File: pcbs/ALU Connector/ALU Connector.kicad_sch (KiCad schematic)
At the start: 4 parts

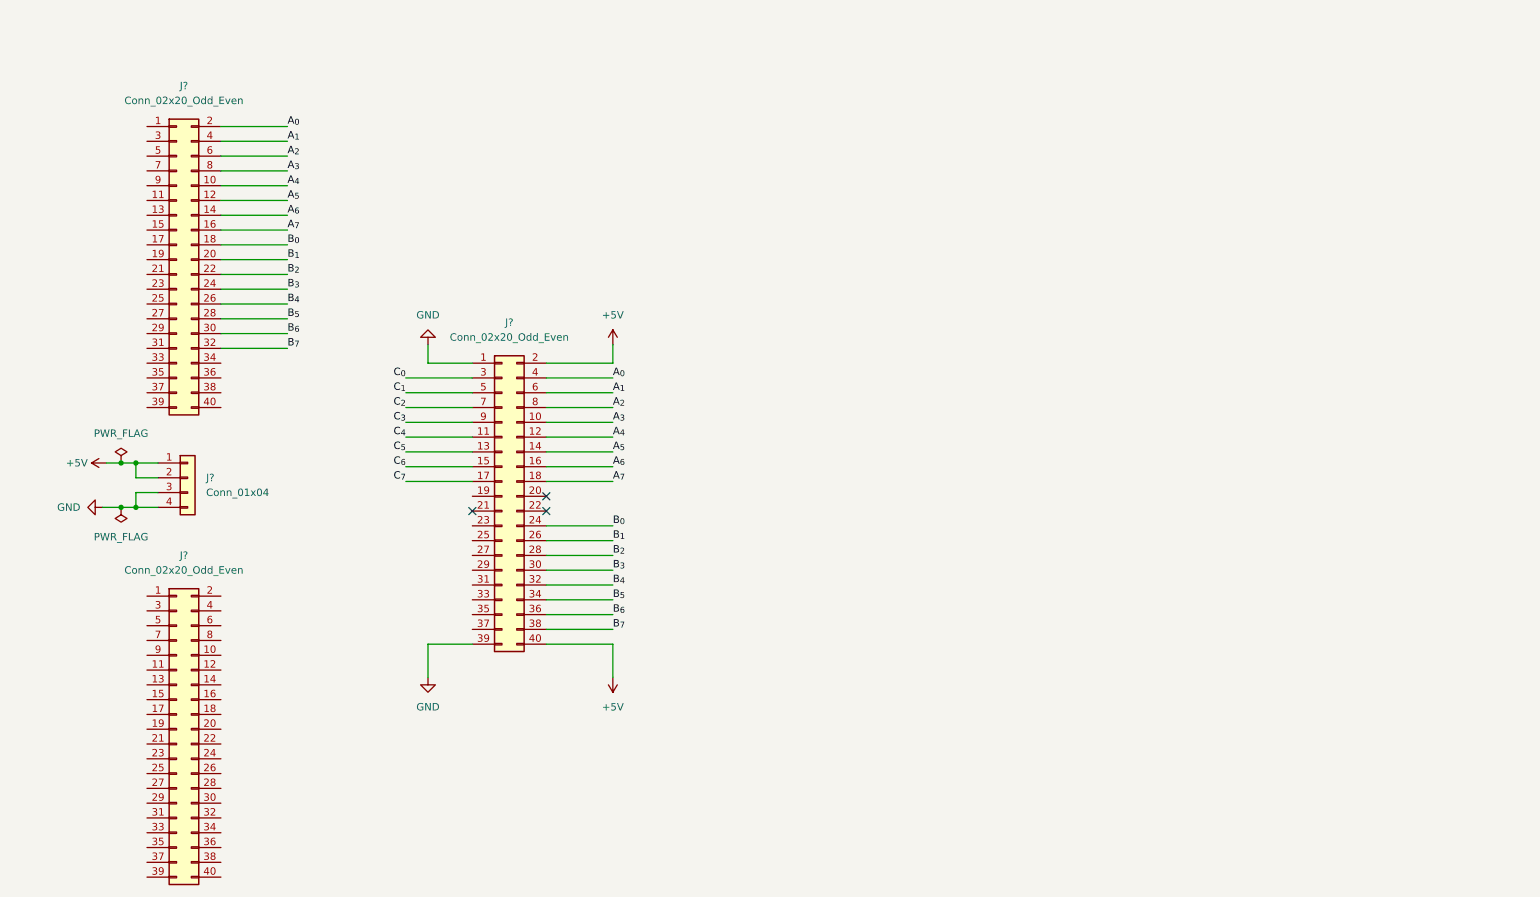
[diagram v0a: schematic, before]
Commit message: Some basic routing
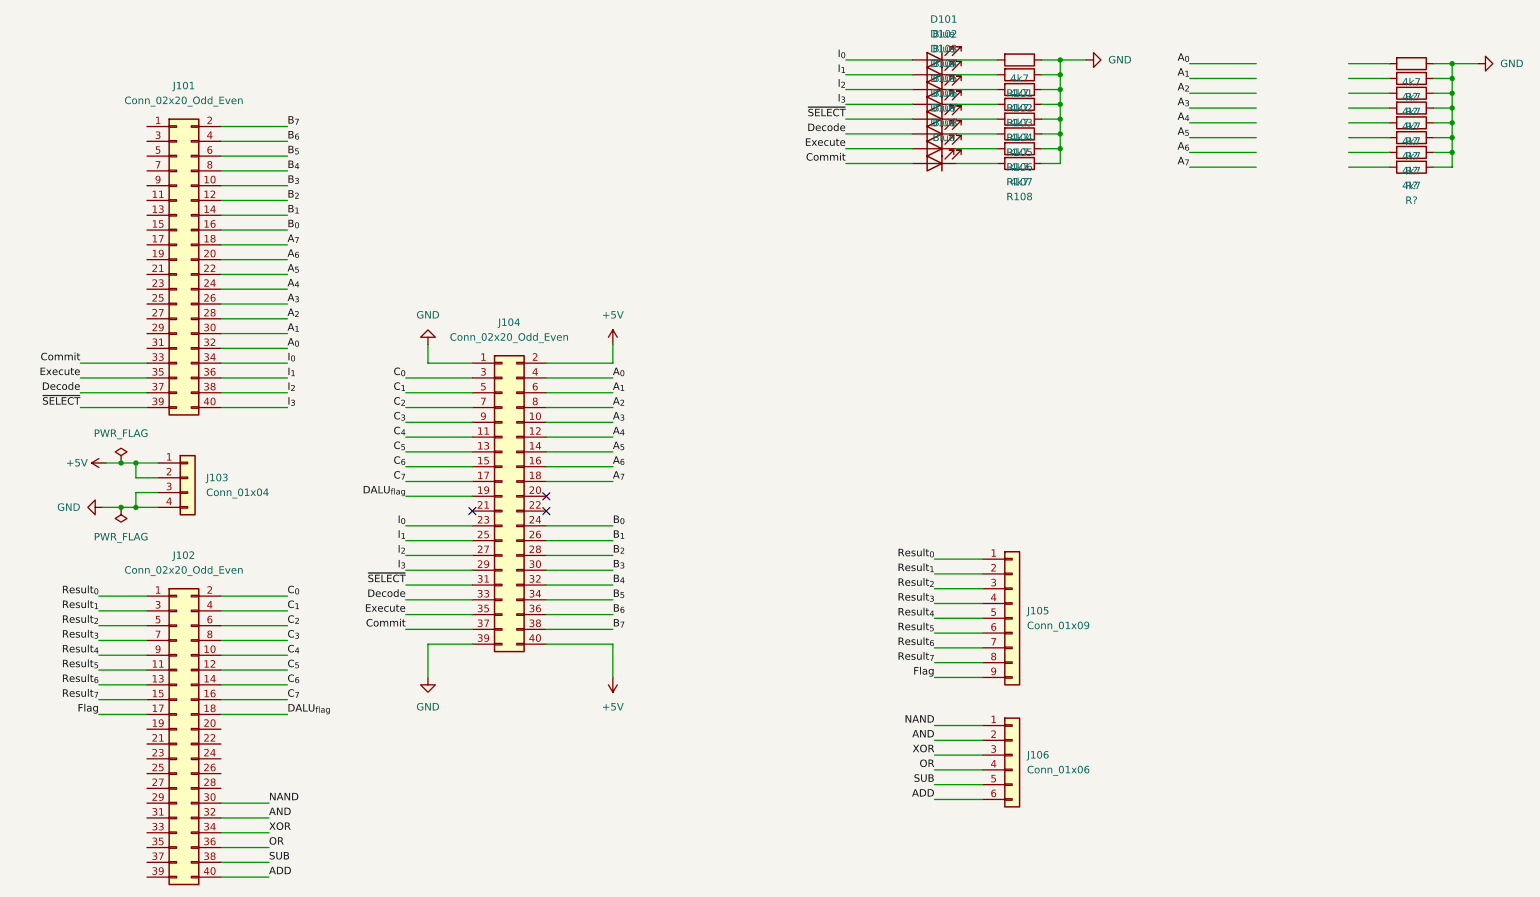
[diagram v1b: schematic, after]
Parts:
- added D101, D102, D103, D104, D105, D106, D107, D108: Blue, LED_SMD:LED_0603_1608Metric, symbol Device:LED
- added J105: Conn_01x09, Connector_PinHeader_2.54mm:PinHeader_1x09_P2.54mm_Vertical, symbol Connector_Generic:Conn_01x09
- added J106: Conn_01x06, Connector_PinHeader_2.54mm:PinHeader_1x06_P2.54mm_Vertical, symbol Connector_Generic:Conn_01x06
- added R101, R102, R103, R104, R105, R106, R107, R108, R? (x8): 4k7, Resistor_SMD:R_0603_1608Metric, symbol Device:R
- J101: renamed from J?; footprint (none) -> Connector_PinHeader_2.54mm:PinHeader_2x20_P2.54mm_Vertical
- J103: renamed from J?; footprint (none) -> Connector_PinHeader_2.54mm:PinHeader_1x04_P2.54mm_Vertical
- gave numbers to parts that had none: 2
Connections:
- net A_{0}: now also J101.32 (Pin_32); no longer J101.2 (Pin_2)
- net A_{1}: now also J101.30 (Pin_30); no longer J101.4 (Pin_4)
- net A_{2}: now also J101.28 (Pin_28); no longer J101.6 (Pin_6)
- net A_{3}: now also J101.26 (Pin_26); no longer J101.8 (Pin_8)
- net A_{4}: now also J101.24 (Pin_24); no longer J101.10 (Pin_10)
- net A_{5}: now also J101.22 (Pin_22); no longer J101.12 (Pin_12)
- net A_{6}: now also J101.20 (Pin_20); no longer J101.14 (Pin_14)
- net A_{7}: now also J101.18 (Pin_18); no longer J101.16 (Pin_16)
- net B_{0}: now also J101.16 (Pin_16); no longer J101.18 (Pin_18)
- net B_{1}: now also J101.14 (Pin_14); no longer J101.20 (Pin_20)
- net B_{2}: now also J101.12 (Pin_12); no longer J101.22 (Pin_22)
- net B_{3}: now also J101.10 (Pin_10); no longer J101.24 (Pin_24)
- net B_{4}: now also J101.8 (Pin_8); no longer J101.26 (Pin_26)
- net B_{5}: now also J101.6 (Pin_6); no longer J101.28 (Pin_28)
- net B_{6}: now also J101.4 (Pin_4); no longer J101.30 (Pin_30)
- net B_{7}: now also J101.2 (Pin_2); no longer J101.32 (Pin_32)
- net C_{0}: now also J102.2 (Pin_2)
- net C_{1}: now also J102.4 (Pin_4)
- net C_{2}: now also J102.6 (Pin_6)
- net C_{3}: now also J102.8 (Pin_8)
- net C_{4}: now also J102.10 (Pin_10)
- net C_{5}: now also J102.12 (Pin_12)
- net C_{6}: now also J102.14 (Pin_14)
- net C_{7}: now also J102.16 (Pin_16)
- net GND: now also R101.1, R102.1, R103.1, R104.1, R105.1, R106.1, R107.1, R108.1, R?.1, R?.1, R?.1, R?.1, R?.1, R?.1, R?.1, R?.1
- net Result_{0}: now reaches J102.1 (Pin_1)
- net Result_{0}: now also J105.1 (Pin_1)
- net Result_{5}: now reaches J102.11 (Pin_11)
- net Result_{5}: now also J105.6 (Pin_6)
- net Result_{6}: now reaches J102.13 (Pin_13)
- net Result_{6}: now also J105.7 (Pin_7)
- net Result_{7}: now reaches J102.15 (Pin_15)
- net Result_{7}: now also J105.8 (Pin_8)
- net Flag: now reaches J102.17 (Pin_17)
- net Flag: now also J105.9 (Pin_9)
- net DALU_{flag}: now reaches J102.18 (Pin_18)
- net DALU_{flag}: now also J104.19 (Pin_19)
- net Result_{1}: now reaches J102.3 (Pin_3)
- net Result_{1}: now also J105.2 (Pin_2)
- net NAND: now reaches J102.30 (Pin_30)
- net NAND: now also J106.1 (Pin_1)
- net AND: now reaches J102.32 (Pin_32)
- net AND: now also J106.2 (Pin_2)
- net XOR: now reaches J102.34 (Pin_34)
- net XOR: now also J106.3 (Pin_3)
- net OR: now reaches J102.36 (Pin_36)
- net OR: now also J106.4 (Pin_4)
- net SUB: now reaches J102.38 (Pin_38)
- net SUB: now also J106.5 (Pin_5)
- net ADD: now reaches J102.40 (Pin_40)
- net ADD: now also J106.6 (Pin_6)
- net Result_{2}: now reaches J102.5 (Pin_5)
- net Result_{2}: now also J105.3 (Pin_3)
- net Result_{3}: now reaches J102.7 (Pin_7)
- net Result_{3}: now also J105.4 (Pin_4)
- net Result_{4}: now reaches J102.9 (Pin_9)
- net Result_{4}: now also J105.5 (Pin_5)
- net I_{0}: now reaches J104.23 (Pin_23)
- net I_{0}: now also J101.34 (Pin_34), D101.2 (A)
- net I_{1}: now reaches J104.25 (Pin_25)
- net I_{1}: now also J101.36 (Pin_36), D102.2 (A)
- net I_{2}: now reaches J104.27 (Pin_27)
- net I_{2}: now also J101.38 (Pin_38), D103.2 (A)
- net I_{3}: now reaches J104.29 (Pin_29)
- net I_{3}: now also J101.40 (Pin_40), D104.2 (A)
- net ~{SELECT}: now reaches J104.31 (Pin_31)
- net ~{SELECT}: now also J101.39 (Pin_39), D105.2 (A)
- net Decode: now reaches J104.33 (Pin_33)
- net Decode: now also J101.37 (Pin_37), D106.2 (A)
- net Execute: now reaches J104.35 (Pin_35)
- net Execute: now also J101.35 (Pin_35), D107.2 (A)
- net Commit: now reaches J104.37 (Pin_37)
- net Commit: now also J101.33 (Pin_33), D108.2 (A)
- new net: D107.1 (K), R107.2
- new net: D105.1 (K), R105.2
- new net: D102.1 (K), R102.2
- new net: D108.1 (K), R108.2
- new net: D101.1 (K), R101.2
- new net: D106.1 (K), R106.2
- new net: D104.1 (K), R104.2
- new net: D103.1 (K), R103.2

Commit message: More routing and LEDs
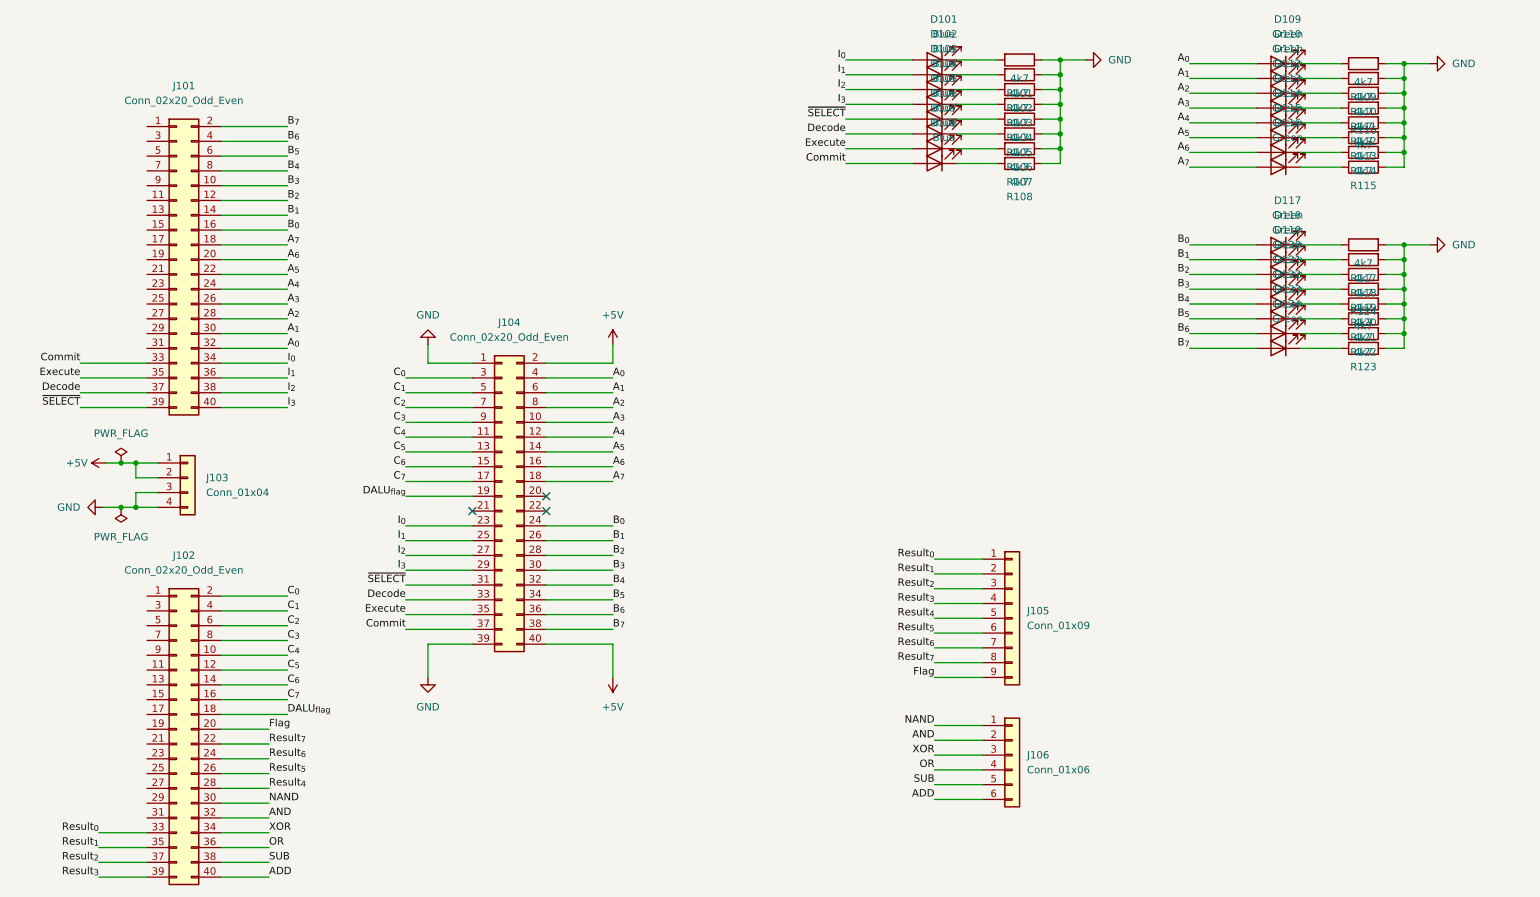
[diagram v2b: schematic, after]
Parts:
- added D109, D110, D111, D112, D113, D114, D115, D116, D117, D118, D119, D120, D121, D122, D123, D124: Green, LED_SMD:LED_0603_1608Metric, symbol Device:LED
- added R117, R118, R119, R120, R121, R122, R123, R124: 4k7, Resistor_SMD:R_0603_1608Metric, symbol Device:R
- gave numbers to parts that had none: 8
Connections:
- net A_{0}: now also D109.2 (A)
- net A_{1}: now also D110.2 (A)
- net A_{2}: now also D111.2 (A)
- net A_{3}: now also D112.2 (A)
- net A_{4}: now also D113.2 (A)
- net A_{5}: now also D114.2 (A)
- net A_{6}: now also D115.2 (A)
- net A_{7}: now also D116.2 (A)
- net B_{0}: now also D117.2 (A)
- net B_{1}: now also D118.2 (A)
- net B_{2}: now also D119.2 (A)
- net B_{3}: now also D120.2 (A)
- net B_{4}: now also D121.2 (A)
- net B_{5}: now also D122.2 (A)
- net B_{6}: now also D123.2 (A)
- net B_{7}: now also D124.2 (A)
- net Flag: now also J102.20 (Pin_20); no longer J102.17 (Pin_17)
- net GND: now also R109.2, R110.2, R111.2, R112.2, R113.2, R114.2, R115.2, R116.2, R117.2, R118.2, R119.2, R120.2, R121.2, R122.2, R123.2, R124.2; no longer R109.1, R110.1, R111.1, R112.1, R113.1, R114.1, R115.1, R116.1
- net Result_{0}: now also J102.33 (Pin_33); no longer J102.1 (Pin_1)
- net Result_{1}: now also J102.35 (Pin_35); no longer J102.3 (Pin_3)
- net Result_{2}: now also J102.37 (Pin_37); no longer J102.5 (Pin_5)
- net Result_{3}: now also J102.39 (Pin_39); no longer J102.7 (Pin_7)
- net Result_{4}: now also J102.28 (Pin_28); no longer J102.9 (Pin_9)
- net Result_{5}: now also J102.26 (Pin_26); no longer J102.11 (Pin_11)
- net Result_{6}: now also J102.24 (Pin_24); no longer J102.13 (Pin_13)
- net Result_{7}: now also J102.22 (Pin_22); no longer J102.15 (Pin_15)
- new net: D112.1 (K), R112.1
- new net: D121.1 (K), R121.1
- new net: D124.1 (K), R124.1
- new net: D109.1 (K), R109.1
- new net: D120.1 (K), R120.1
- new net: D111.1 (K), R111.1
- new net: D117.1 (K), R117.1
- new net: D123.1 (K), R123.1
- new net: D114.1 (K), R114.1
- new net: D122.1 (K), R122.1
- new net: D110.1 (K), R110.1
- new net: D116.1 (K), R116.1
- new net: D119.1 (K), R119.1
- new net: D113.1 (K), R113.1
- new net: D118.1 (K), R118.1
- new net: D115.1 (K), R115.1
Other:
- moved on the sheet: R109, R110, R111, R112, R113, R114, R115, R116

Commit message: Realised a mistake
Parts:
- removed J105: Conn_01x09, Connector_PinHeader_2.54mm:PinHeader_1x09_P2.54mm_Vertical, symbol Connector_Generic:Conn_01x09
- removed J106: Conn_01x06, Connector_PinHeader_2.54mm:PinHeader_1x06_P2.54mm_Vertical, symbol Connector_Generic:Conn_01x06
- added J105, J106, J107: Conn_01x10, Connector_PinHeader_2.54mm:PinHeader_1x10_P2.54mm_Vertical, symbol Connector_Generic:Conn_01x10
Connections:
- net C_{0}: now also J102.1 (Pin_1); no longer J102.2 (Pin_2)
- net C_{1}: now also J102.2 (Pin_2); no longer J102.4 (Pin_4)
- net C_{2}: now also J102.3 (Pin_3); no longer J102.6 (Pin_6)
- net C_{3}: now also J102.4 (Pin_4); no longer J102.8 (Pin_8)
- net C_{4}: now also J102.5 (Pin_5); no longer J102.10 (Pin_10)
- net C_{5}: now also J102.6 (Pin_6); no longer J102.12 (Pin_12)
- net C_{6}: now also J102.7 (Pin_7); no longer J102.14 (Pin_14)
- net C_{7}: now also J102.8 (Pin_8); no longer J102.16 (Pin_16)
- net DALU_{flag}: now also J102.9 (Pin_9); no longer J102.18 (Pin_18)
- net In_{08}: now reaches J102.11 (Pin_11)
- net In_{08}: now also J105.9 (Pin_9)
- net In_{06}: now reaches J102.13 (Pin_13)
- net In_{06}: now also J105.7 (Pin_7)
- net In_{05}: now reaches J102.15 (Pin_15)
- net In_{05}: now also J105.6 (Pin_6)
- net In_{03}: now reaches J102.17 (Pin_17)
- net In_{03}: now also J105.4 (Pin_4)
- net In_{01}: now reaches J102.19 (Pin_19)
- net In_{01}: now also J105.2 (Pin_2)
- net ADD: no longer names the net of J102.40 (Pin_40)
- net AND: no longer names the net of J102.32 (Pin_32)
- net Flag renamed In_{00}
- net In_{00}: now also J105.1 (Pin_1)
- net NAND: no longer names the net of J102.30 (Pin_30)
- net OR: no longer names the net of J102.36 (Pin_36)
- net Result_{0}: no longer names the net of J102.33 (Pin_33)
- net Result_{1}: no longer names the net of J102.35 (Pin_35)
- net Result_{2}: no longer names the net of J102.37 (Pin_37)
- net Result_{3}: no longer names the net of J102.39 (Pin_39)
- net Result_{4}: no longer names the net of J102.28 (Pin_28)
- net Result_{5}: no longer names the net of J102.26 (Pin_26)
- net Result_{6}: no longer names the net of J102.24 (Pin_24)
- net Result_{7}: no longer names the net of J102.22 (Pin_22)
- net SUB: no longer names the net of J102.38 (Pin_38)
- net XOR: no longer names the net of J102.34 (Pin_34)
- new net In_{02}: J102.18 (Pin_18), J105.3 (Pin_3)
- new net In_{04}: J102.16 (Pin_16), J105.5 (Pin_5)
- new net In_{07}: J102.14 (Pin_14), J105.8 (Pin_8)
- new net In_{09}: J102.12 (Pin_12), J105.10 (Pin_10)

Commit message: Finished draft
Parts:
- added D125, D126, D127, D128, D129, D130, D131, D132, D133: Yellow, LED_SMD:LED_0603_1608Metric, symbol Device:LED
- added R125, R126, R127, R128, R129, R130, R131, R132, R133: 4k7, Resistor_SMD:R_0603_1608Metric, symbol Device:R
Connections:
- net C_{0}: now also D125.2 (A)
- net C_{1}: now also D126.2 (A)
- net C_{2}: now also D127.2 (A)
- net C_{3}: now also D128.2 (A)
- net C_{4}: now also D129.2 (A)
- net C_{5}: now also D130.2 (A)
- net C_{6}: now also D131.2 (A)
- net C_{7}: now also D132.2 (A)
- net DALU_{flag}: now also D133.2 (A)
- net GND: now also R125.2, R126.2, R127.2, R128.2, R129.2, R130.2, R131.2, R132.2, R133.2
- net In_{10}: now reaches J106.1 (Pin_1)
- net In_{10}: now also J102.30 (Pin_30)
- net In_{19}: now reaches J106.10 (Pin_10)
- net In_{19}: now also J102.22 (Pin_22)
- net In_{11}: now reaches J106.2 (Pin_2)
- net In_{11}: now also J102.29 (Pin_29)
- net In_{12}: now reaches J106.3 (Pin_3)
- net In_{12}: now also J102.28 (Pin_28)
- net In_{13}: now reaches J106.4 (Pin_4)
- net In_{13}: now also J102.27 (Pin_27)
- net In_{14}: now reaches J106.5 (Pin_5)
- net In_{14}: now also J102.26 (Pin_26)
- net In_{15}: now reaches J106.6 (Pin_6)
- net In_{15}: now also J102.25 (Pin_25)
- net In_{16}: now reaches J106.7 (Pin_7)
- net In_{16}: now also J102.23 (Pin_23)
- net In_{17}: now reaches J106.8 (Pin_8)
- net In_{17}: now also J102.24 (Pin_24)
- net In_{18}: now reaches J106.9 (Pin_9)
- net In_{18}: now also J102.21 (Pin_21)
- net In_{28}: now reaches J102.31 (Pin_31)
- net In_{28}: now also J107.9 (Pin_9)
- net In_{29}: now reaches J102.32 (Pin_32)
- net In_{29}: now also J107.10 (Pin_10)
- net In_{26}: now reaches J102.33 (Pin_33)
- net In_{26}: now also J107.7 (Pin_7)
- net In_{27}: now reaches J102.34 (Pin_34)
- net In_{27}: now also J107.8 (Pin_8)
- net In_{25}: now reaches J102.35 (Pin_35)
- net In_{25}: now also J107.6 (Pin_6)
- net In_{24}: now reaches J102.36 (Pin_36)
- net In_{24}: now also J107.5 (Pin_5)
- net In_{23}: now reaches J102.37 (Pin_37)
- net In_{23}: now also J107.4 (Pin_4)
- net In_{22}: now reaches J102.38 (Pin_38)
- net In_{22}: now also J107.3 (Pin_3)
- net In_{21}: now reaches J102.39 (Pin_39)
- net In_{21}: now also J107.2 (Pin_2)
- net In_{20}: now reaches J102.40 (Pin_40)
- net In_{20}: now also J107.1 (Pin_1)
- new net: D133.1 (K), R133.1
- new net: D126.1 (K), R126.1
- new net: D127.1 (K), R127.1
- new net: D129.1 (K), R129.1
- new net: D132.1 (K), R132.1
- new net: D128.1 (K), R128.1
- new net: D130.1 (K), R130.1
- new net: D125.1 (K), R125.1
- new net: D131.1 (K), R131.1
- no-connect marks 3 -> 20
